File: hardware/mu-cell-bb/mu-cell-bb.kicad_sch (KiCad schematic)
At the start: 73 parts, among them IC1 SX1255, J1 TX, J2 RX, J3 EXT_CLK, J4 RPi GPIO, J5 IO, Q1 BC817-40W, Q2 BC817-40W, U1 24LC256, U2 LDK130M33R, Y1 32MHz

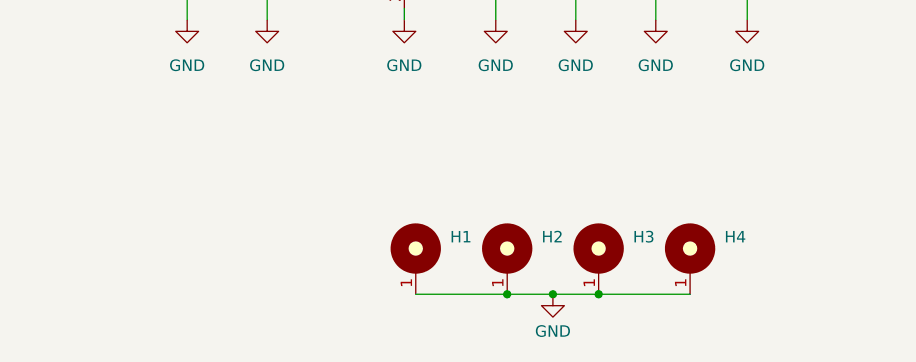
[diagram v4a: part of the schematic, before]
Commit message: added PCB changes and parts
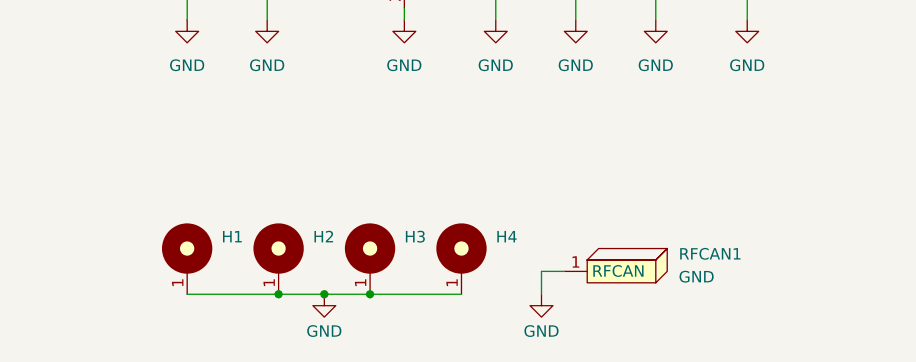
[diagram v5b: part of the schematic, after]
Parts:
- added RFCAN1: GND, parts:2118707-4 CAN, symbol parts:RFCAN
- J5: footprint Connector_IDC:IDC-Header_2x06_P2.54mm_Vertical -> Connector_IDC:IDC-Header_2x06_P2.54mm_Horizontal
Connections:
- net GND: now also RFCAN1.1 (RFCAN)
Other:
- moved on the sheet: H1, H2, H3, H4
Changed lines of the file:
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@@
 	)
 	(junction
-		(at 148.59 186.69)
+		(at 123.19 186.69)
 		(diameter 0)
 		(color 0 0 0 0)
 	)
 	(junction
-		(at 138.43 186.69)
+		(at 113.03 186.69)
 		(diameter 0)
 		(color 0 0 0 0)
@@
 	)
 	(junction
-		(at 143.51 186.69)
+		(at 118.11 186.69)
 		(diameter 0)
 		(color 0 0 0 0)
@@
 	(wire
 		(pts
+			(xy 142.24 184.15) (xy 144.78 184.15)
+		)
+		(stroke
+			(width 0)
+			(type default)
+		)
+	)
+	(wire
+		(pts
 			(xy 40.64 60.96) (xy 40.64 64.77)
 		)
@@
 	(wire
 		(pts
-			(xy 148.59 186.69) (xy 158.75 186.69)
+			(xy 123.19 186.69) (xy 133.35 186.69)
 		)
 		(stroke
@@
 	(wire
 		(pts
+			(xy 142.24 186.69) (xy 142.24 184.15)
+		)
+		(stroke
+			(width 0)
+			(type default)
+		)
+	)
+	(wire
+		(pts
 			(xy 163.83 76.2) (xy 179.07 76.2)
 		)
@@
 	(wire
 		(pts
-			(xy 138.43 186.69) (xy 143.51 186.69)
+			(xy 113.03 186.69) (xy 118.11 186.69)
 		)
 		(stroke
@@
 	(wire
 		(pts
-			(xy 128.27 186.69) (xy 138.43 186.69)
+			(xy 102.87 186.69) (xy 113.03 186.69)
 		)
 		(stroke
@@
 	(wire
 		(pts
-			(xy 143.51 186.69) (xy 148.59 186.69)
+			(xy 118.11 186.69) (xy 123.19 186.69)
 		)
 		(stroke
@@
 	(symbol
 		(lib_id "PCM_SL_Mechanical:MountingHole_M3_3.2mm_Pad")
-		(at 148.59 181.61 0)
+		(at 123.19 181.61 0)
 		(unit 1)
 		(exclude_from_sim no)
@@
 		(fields_autoplaced yes)
 		(property "Reference" "H3"
-			(at 152.4 180.3399 0)
+			(at 127 180.3399 0)
 			(effects
 				(font
@@
 		)
 		(property "Value" "MountingHole_M3_3.2mm_Pad"
-			(at 152.4 182.8799 0)
+			(at 127 182.8799 0)
 			(effects
 				(font
@@
 		)
 		(property "Footprint" "MountingHole:MountingHole_3.2mm_M3_DIN965_Pad"
-			(at 148.59 185.42 0)
+			(at 123.19 185.42 0)
 			(effects
 				(font
@@
 		)
 		(property "Datasheet" ""
-			(at 148.59 181.61 0)
+			(at 123.19 181.61 0)
 			(effects
 				(font
@@
 		)
 		(property "Description" "3.2mm Diameter Mounting Hole Pad (M3)"
-			(at 148.59 181.61 0)
+			(at 123.19 181.61 0)
 			(effects
 				(font
@@
 	(symbol
 		(lib_id "PCM_SL_Mechanical:MountingHole_M3_3.2mm_Pad")
-		(at 128.27 181.61 0)
+		(at 102.87 181.61 0)
 		(unit 1)
 		(exclude_from_sim no)
@@
 		(fields_autoplaced yes)
 		(property "Reference" "H1"
-			(at 132.08 180.3399 0)
+			(at 106.68 180.3399 0)
 			(effects
 				(font
@@
 		)
 		(property "Value" "MountingHole_M3_3.2mm_Pad"
-			(at 132.08 182.8799 0)
+			(at 106.68 182.8799 0)
 			(effects
 				(font
@@
 		)
 		(property "Footprint" "MountingHole:MountingHole_3.2mm_M3_DIN965_Pad"
-			(at 128.27 185.42 0)
+			(at 102.87 185.42 0)
 			(effects
 				(font
@@
 		)
 		(property "Datasheet" ""
-			(at 128.27 181.61 0)
+			(at 102.87 181.61 0)
 			(effects
 				(font
@@
 		)
 		(property "Description" "3.2mm Diameter Mounting Hole Pad (M3)"
-			(at 128.27 181.61 0)
+			(at 102.87 181.61 0)
 			(effects
 				(font
@@
 	(symbol
 		(lib_id "power:GND")
-		(at 143.51 186.69 0)
+		(at 118.11 186.69 0)
 		(unit 1)
 		(exclude_from_sim no)
@@
 		(fields_autoplaced yes)
 		(property "Reference" "#PWR044"
-			(at 143.51 193.04 0)
+			(at 118.11 193.04 0)
 			(effects
 				(font
@@
 		)
 		(property "Value" "GND"
-			(at 143.51 190.8231 0)
+			(at 118.11 190.8231 0)
 			(effects
 				(font
@@
 		)
 		(property "Footprint" ""
-			(at 143.51 186.69 0)
+			(at 118.11 186.69 0)
 			(effects
 				(font
@@
 		)
 		(property "Datasheet" ""
-			(at 143.51 186.69 0)
+			(at 118.11 186.69 0)
 			(effects
 				(font
@@
 		)
 		(property "Description" "Power symbol creates a global label with name \"GND\" , ground"
-			(at 143.51 186.69 0)
+			(at 118.11 186.69 0)
 			(effects
 				(font
@@
 	)
 	(symbol
+		(lib_id "power:GND")
+		(at 142.24 186.69 0)
+		(unit 1)
+		(exclude_from_sim no)
+		(in_bom yes)
+		(on_board yes)
+		(dnp no)
+		(fields_autoplaced yes)
+		(property "Reference" "#PWR061"
+			(at 142.24 193.04 0)
+			(effects
+				(font
+					(size 1.27 1.27)
+				)
+				(hide yes)
+			)
+		)
+		(property "Value" "GND"
+			(at 142.24 190.8231 0)
+			(effects
+				(font
+					(size 1.27 1.27)
+				)
+			)
+		)
+		(property "Footprint" ""
+			(at 142.24 186.69 0)
+			(effects
+				(font
+					(size 1.27 1.27)
+				)
+				(hide yes)
+			)
+		)
+		(property "Datasheet" ""
+			(at 142.24 186.69 0)
+			(effects
+				(font
+					(size 1.27 1.27)
+				)
+				(hide yes)
+			)
+		)
+		(property "Description" "Power symbol creates a global label with name \"GND\" , ground"
+			(at 142.24 186.69 0)
+			(effects
+				(font
+					(size 1.27 1.27)
+				)
+				(hide yes)
+			)
+		)
+		(pin "1"
+		)
+		(instances
+			(project "mu-cell-bb"
+				(path "/564c8f3e-4a0a-4bb3-921f-1318a09780f9"
+					(reference "#PWR061")
+					(unit 1)
+				)
+			)
+		)
+	)
+	(symbol
 		(lib_id "Device:C_Small")
 		(at 102.87 36.83 0)
@@
 	(symbol
 		(lib_id "PCM_SL_Mechanical:MountingHole_M3_3.2mm_Pad")
-		(at 138.43 181.61 0)
+		(at 113.03 181.61 0)
 		(unit 1)
 		(exclude_from_sim no)
@@
 		(fields_autoplaced yes)
 		(property "Reference" "H2"
-			(at 142.24 180.3399 0)
+			(at 116.84 180.3399 0)
 			(effects
 				(font
@@
 		)
 		(property "Value" "MountingHole_M3_3.2mm_Pad"
-			(at 142.24 182.8799 0)
+			(at 116.84 182.8799 0)
 			(effects
 				(font
@@
 		)
 		(property "Footprint" "MountingHole:MountingHole_3.2mm_M3_DIN965_Pad"
-			(at 138.43 185.42 0)
+			(at 113.03 185.42 0)
 			(effects
 				(font
@@
 		)
 		(property "Datasheet" ""
-			(at 138.43 181.61 0)
+			(at 113.03 181.61 0)
 			(effects
 				(font
@@
 		)
 		(property "Description" "3.2mm Diameter Mounting Hole Pad (M3)"
-			(at 138.43 181.61 0)
+			(at 113.03 181.61 0)
 			(effects
 				(font
@@
 	)
 	(symbol
+		(lib_id "parts:RFCAN")
+		(at 151.13 184.15 0)
+		(unit 1)
+		(exclude_from_sim no)
+		(in_bom yes)
+		(on_board yes)
+		(dnp no)
+		(fields_autoplaced yes)
+		(property "Reference" "RFCAN1"
+			(at 157.48 182.2449 0)
+			(effects
+				(font
+					(size 1.27 1.27)
+				)
+				(justify left)
+			)
+		)
+		(property "Value" "GND"
+			(at 157.48 184.7849 0)
+			(effects
+				(font
+					(size 1.27 1.27)
+				)
+				(justify left)
+			)
+		)
+		(property "Footprint" "parts:2118707-4 CAN"
+			(at 151.13 184.15 0)
+			(effects
+				(font
+					(size 1.27 1.27)
+				)
+				(hide yes)
+			)
+		)
+		(property "Datasheet" ""
+			(at 151.13 184.15 0)
+			(effects
+				(font
+					(size 1.27 1.27)
+				)
+				(hide yes)
+			)
+		)
+		(property "Description" ""
+			(at 151.13 184.15 0)
+			(effects
+				(font
+					(size 1.27 1.27)
+				)
+				(hide yes)
+			)
+		)
+		(pin "1"
+		)
+		(instances
+			(project ""
+				(path "/564c8f3e-4a0a-4bb3-921f-1318a09780f9"
+					(reference "RFCAN1")
+					(unit 1)
+				)
+			)
+		)
+	)
+	(symbol
 		(lib_id "power:GND")
 		(at 30.48 40.64 0)
@@
 	(symbol
 		(lib_id "PCM_SL_Mechanical:MountingHole_M3_3.2mm_Pad")
-		(at 158.75 181.61 0)
+		(at 133.35 181.61 0)
 		(unit 1)
 		(exclude_from_sim no)
@@
 		(fields_autoplaced yes)
 		(property "Reference" "H4"
-			(at 162.56 180.3399 0)
+			(at 137.16 180.3399 0)
 			(effects
 				(font
@@
 		)
 		(property "Value" "MountingHole_M3_3.2mm_Pad"
-			(at 162.56 182.8799 0)
+			(at 137.16 182.8799 0)
 			(effects
 				(font
@@
 		)
 		(property "Footprint" "MountingHole:MountingHole_3.2mm_M3_DIN965_Pad"
-			(at 158.75 185.42 0)
+			(at 133.35 185.42 0)
 			(effects
 				(font
@@
 		)
 		(property "Datasheet" ""
-			(at 158.75 181.61 0)
+			(at 133.35 181.61 0)
 			(effects
 				(font
@@
 		)
 		(property "Description" "3.2mm Diameter Mounting Hole Pad (M3)"
-			(at 158.75 181.61 0)
+			(at 133.35 181.61 0)
 			(effects
 				(font
@@
 			)
 		)
-		(property "Footprint" "Connector_IDC:IDC-Header_2x06_P2.54mm_Vertical"
+		(property "Footprint" "Connector_IDC:IDC-Header_2x06_P2.54mm_Horizontal"
 			(at 247.65 69.85 0)
 			(effects

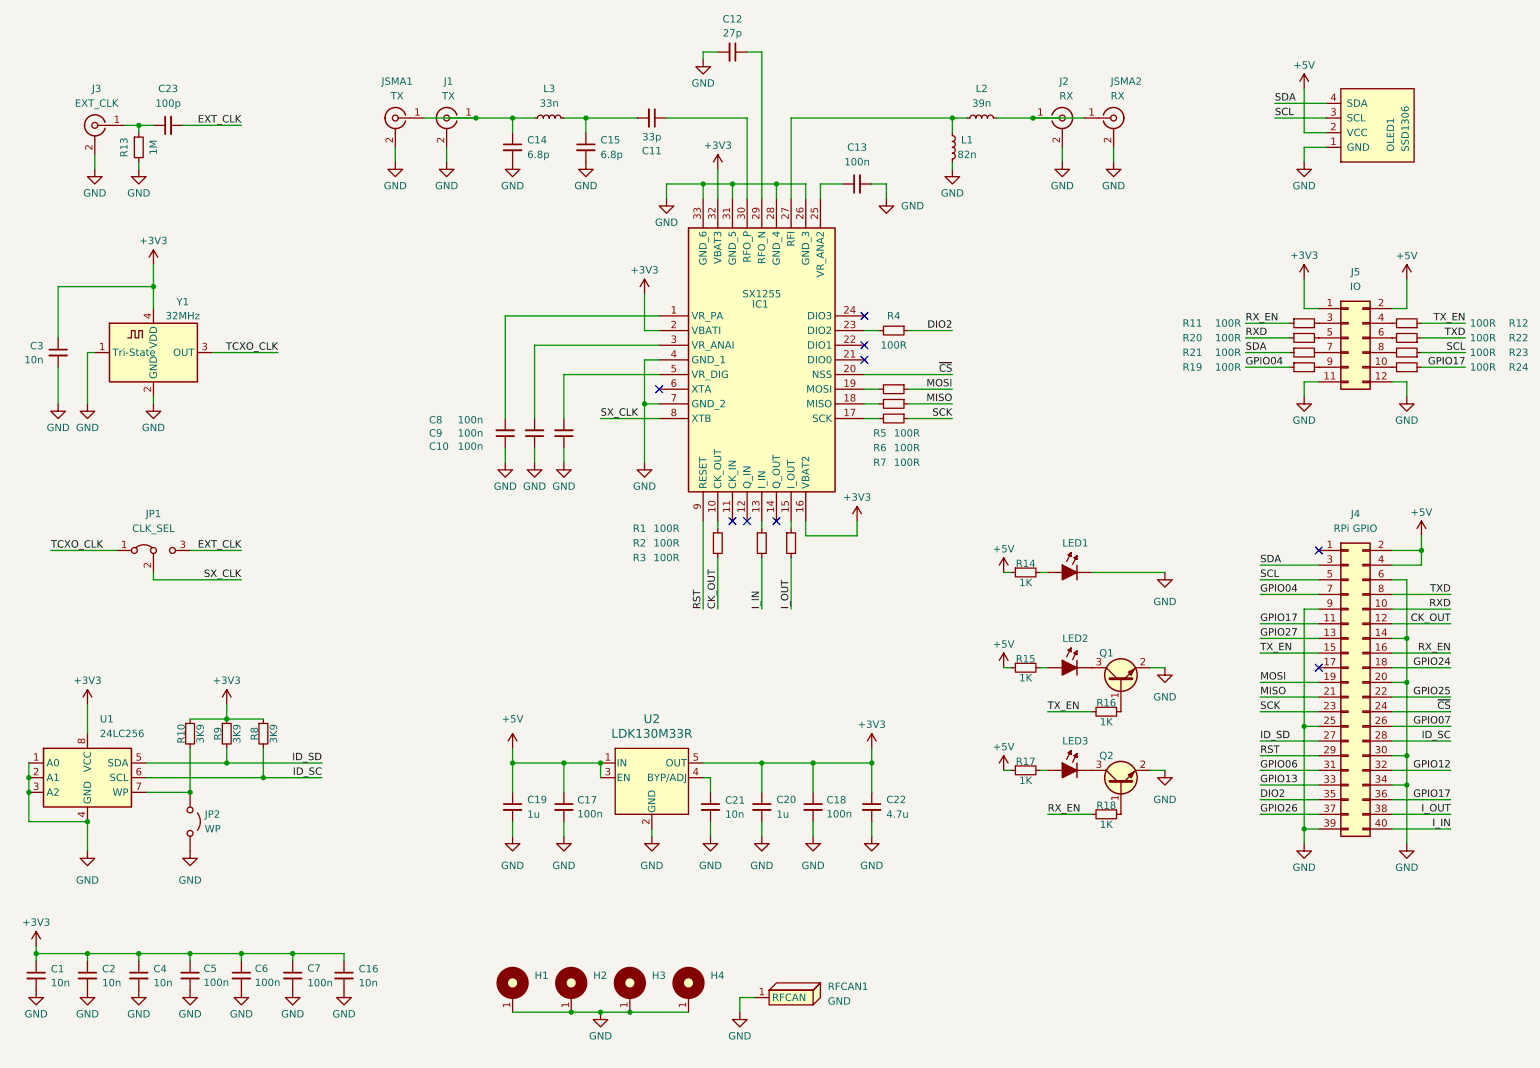
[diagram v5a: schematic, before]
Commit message: updated footprints
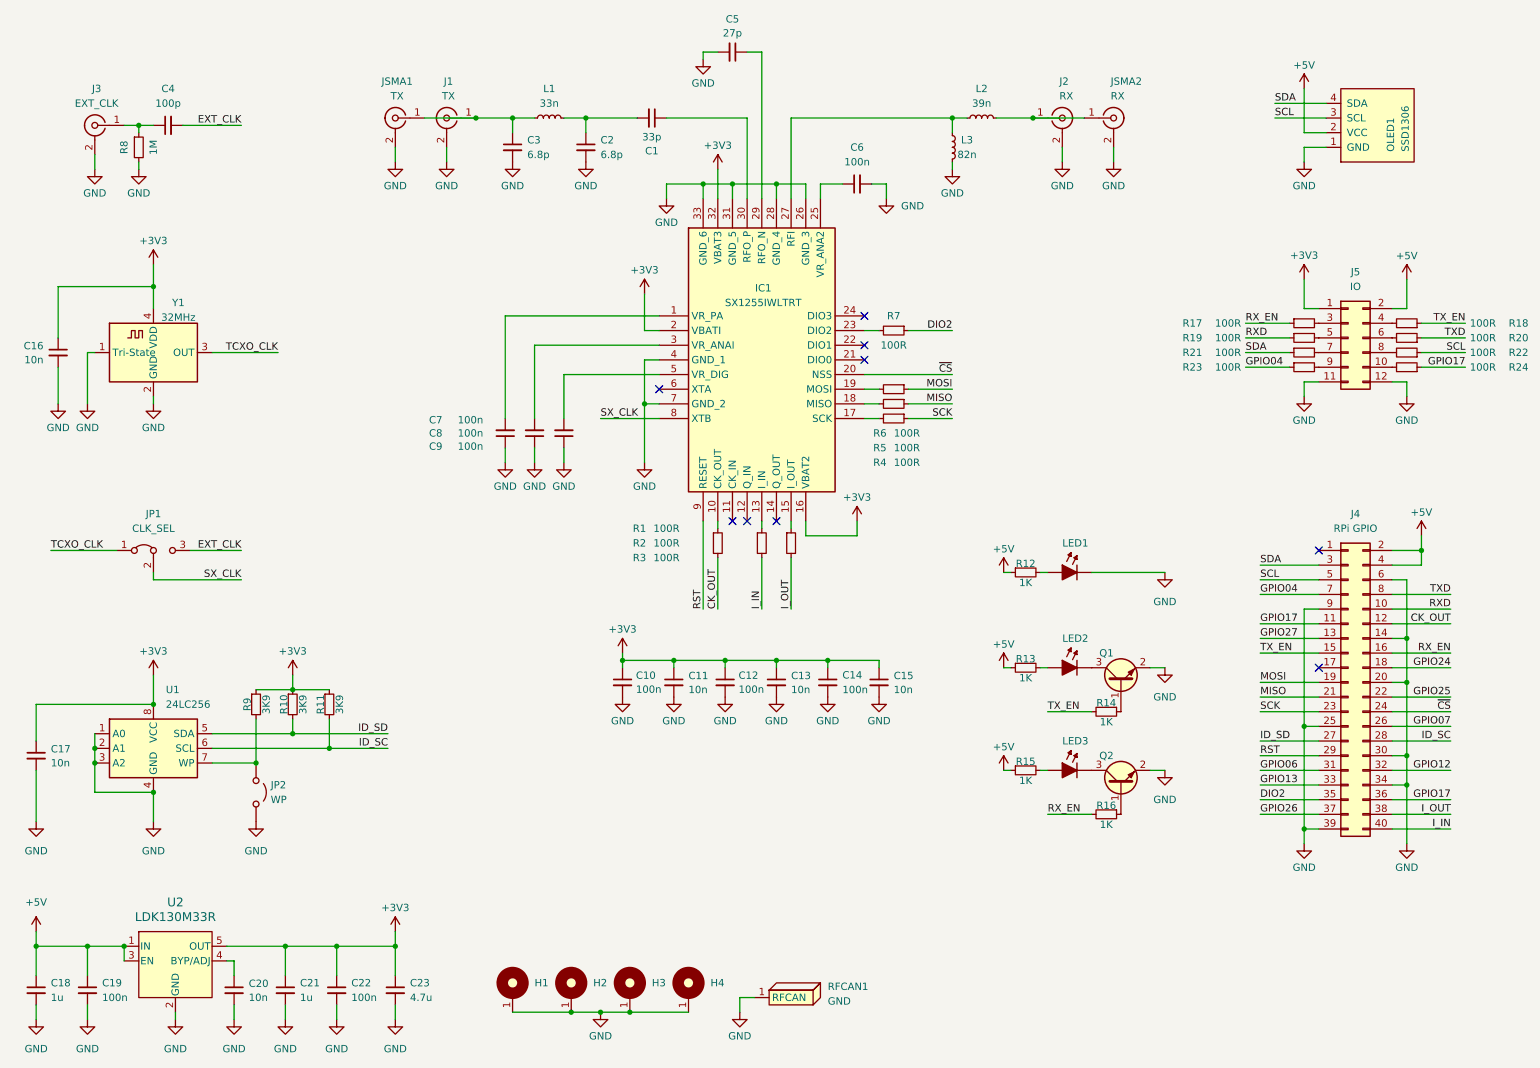
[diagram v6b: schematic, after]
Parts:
- removed C16, C2, C4: 10n, Capacitor_SMD:C_0603_1608Metric, symbol Device:C_Small
- removed C5, C6, C7: 100n, Capacitor_SMD:C_0603_1608Metric, symbol Device:C_Small
- removed IC1: SX1255, parts:QFN50P500X500X80-33N-D, symbol SX1255:SX1255IWLTRT
- removed Y1: 32MHz, Oscillator:Oscillator_SMD_ECS_2520MV-xxx-xx-4Pin_2.5x2.0mm, symbol Oscillator:ECS-2520MV-xxx-xx
- added C10, C12, C14: 100n, Capacitor_SMD:C_0402_1005Metric_Pad0.74x0.62mm_HandSolder, symbol Device:C_Small
- added C13, C15, C17: 10n, Capacitor_SMD:C_0402_1005Metric_Pad0.74x0.62mm_HandSolder, symbol Device:C_Small
- added IC1: SX1255IWLTRT, parts:QFN50P500X500X80-33N-D, symbol parts:SX1255IWLTRT
- added Y1: 32MHz, parts:Oscillator_SMD_ECS_2520MV-xxx-xx-4Pin_2.5x2.0mm, symbol parts:ECS-2520MV-xxx-xx
- C1: renamed from C11; footprint Capacitor_SMD:C_0603_1608Metric -> Capacitor_SMD:C_0402_1005Metric_Pad0.74x0.62mm_HandSolder
- C11: renamed from C1; footprint Capacitor_SMD:C_0603_1608Metric -> Capacitor_SMD:C_0402_1005Metric_Pad0.74x0.62mm_HandSolder
- C16: renamed from C3; footprint Capacitor_SMD:C_0603_1608Metric -> Capacitor_SMD:C_0402_1005Metric_Pad0.74x0.62mm_HandSolder
- C18: renamed from C19; footprint Capacitor_SMD:C_0603_1608Metric -> Capacitor_SMD:C_0402_1005Metric_Pad0.74x0.62mm_HandSolder
- C19: renamed from C17; footprint Capacitor_SMD:C_0603_1608Metric -> Capacitor_SMD:C_0402_1005Metric_Pad0.74x0.62mm_HandSolder
- C2: renamed from C15; footprint Capacitor_SMD:C_0603_1608Metric -> Capacitor_SMD:C_0402_1005Metric_Pad0.74x0.62mm_HandSolder
- C20: renamed from C21; footprint Capacitor_SMD:C_0603_1608Metric -> Capacitor_SMD:C_0402_1005Metric_Pad0.74x0.62mm_HandSolder
- C21: renamed from C20; footprint Capacitor_SMD:C_0603_1608Metric -> Capacitor_SMD:C_0402_1005Metric_Pad0.74x0.62mm_HandSolder
- C22: renamed from C18; footprint Capacitor_SMD:C_0603_1608Metric -> Capacitor_SMD:C_0402_1005Metric_Pad0.74x0.62mm_HandSolder
- C23: renamed from C22; footprint Capacitor_SMD:C_0603_1608Metric -> Capacitor_SMD:C_0402_1005Metric_Pad0.74x0.62mm_HandSolder
- C3: renamed from C14; footprint Capacitor_SMD:C_0603_1608Metric -> Capacitor_SMD:C_0402_1005Metric_Pad0.74x0.62mm_HandSolder
- C4: renamed from C23; footprint Capacitor_SMD:C_0603_1608Metric -> Capacitor_SMD:C_0402_1005Metric_Pad0.74x0.62mm_HandSolder
- C5: renamed from C12; footprint Capacitor_SMD:C_0603_1608Metric -> Capacitor_SMD:C_0402_1005Metric_Pad0.74x0.62mm_HandSolder
- C6: renamed from C13; footprint Capacitor_SMD:C_0603_1608Metric -> Capacitor_SMD:C_0402_1005Metric_Pad0.74x0.62mm_HandSolder
- C7: renamed from C8; footprint Capacitor_SMD:C_0603_1608Metric -> Capacitor_SMD:C_0402_1005Metric_Pad0.74x0.62mm_HandSolder
- C8: renamed from C9; footprint Capacitor_SMD:C_0603_1608Metric -> Capacitor_SMD:C_0402_1005Metric_Pad0.74x0.62mm_HandSolder
- C9: renamed from C10; footprint Capacitor_SMD:C_0603_1608Metric -> Capacitor_SMD:C_0402_1005Metric_Pad0.74x0.62mm_HandSolder
- H1, H2, H3, H4: footprint MountingHole:MountingHole_3.2mm_M3_DIN965_Pad -> PCM_SL_Mechanical:MountingHole_3.2mm_Pad
- J3: footprint (none) -> parts:U.FL_Vertical_GND
- L1: renamed from L3; footprint Inductor_SMD:L_0603_1608Metric -> Inductor_SMD:L_0402_1005Metric_Pad0.77x0.64mm_HandSolder
- L2: footprint Inductor_SMD:L_0603_1608Metric -> Inductor_SMD:L_0402_1005Metric_Pad0.77x0.64mm_HandSolder
- L3: renamed from L1; footprint Inductor_SMD:L_0603_1608Metric -> Inductor_SMD:L_0402_1005Metric_Pad0.77x0.64mm_HandSolder
- LED1, LED2, LED3: footprint LED_SMD:LED_0603_1608Metric -> PCM_LED_SMD_AKL:LED_0402_1005Metric_Pad0.77x0.64mm
- Q1, Q2: footprint Package_TO_SOT_SMD:SOT-323_SC-70_Handsoldering -> Package_TO_SOT_SMD:SOT-323_SC-70
- R1, R2, R21, R24, R3: footprint Resistor_SMD:R_0603_1608Metric -> Resistor_SMD:R_0402_1005Metric_Pad0.72x0.64mm_HandSolder
- R10: renamed from R9; footprint Resistor_SMD:R_0603_1608Metric -> Resistor_SMD:R_0402_1005Metric_Pad0.72x0.64mm_HandSolder
- R11: renamed from R8; footprint Resistor_SMD:R_0603_1608Metric -> Resistor_SMD:R_0402_1005Metric_Pad0.72x0.64mm_HandSolder
- R12: renamed from R14; footprint Resistor_SMD:R_0603_1608Metric -> Resistor_SMD:R_0402_1005Metric_Pad0.72x0.64mm_HandSolder
- R13: renamed from R15; footprint Resistor_SMD:R_0603_1608Metric -> Resistor_SMD:R_0402_1005Metric_Pad0.72x0.64mm_HandSolder
- R14: renamed from R16; footprint Resistor_SMD:R_0603_1608Metric -> Resistor_SMD:R_0402_1005Metric_Pad0.72x0.64mm_HandSolder
- R15: renamed from R17; footprint Resistor_SMD:R_0603_1608Metric -> Resistor_SMD:R_0402_1005Metric_Pad0.72x0.64mm_HandSolder
- R16: renamed from R18; footprint Resistor_SMD:R_0603_1608Metric -> Resistor_SMD:R_0402_1005Metric_Pad0.72x0.64mm_HandSolder
- R17: renamed from R11; footprint Resistor_SMD:R_0603_1608Metric -> Resistor_SMD:R_0402_1005Metric_Pad0.72x0.64mm_HandSolder
- R18: renamed from R12; footprint Resistor_SMD:R_0603_1608Metric -> Resistor_SMD:R_0402_1005Metric_Pad0.72x0.64mm_HandSolder
- R19: renamed from R20; footprint Resistor_SMD:R_0603_1608Metric -> Resistor_SMD:R_0402_1005Metric_Pad0.72x0.64mm_HandSolder
- R20: renamed from R22; footprint Resistor_SMD:R_0603_1608Metric -> Resistor_SMD:R_0402_1005Metric_Pad0.72x0.64mm_HandSolder
- R22: renamed from R23; footprint Resistor_SMD:R_0603_1608Metric -> Resistor_SMD:R_0402_1005Metric_Pad0.72x0.64mm_HandSolder
- R23: renamed from R19; footprint Resistor_SMD:R_0603_1608Metric -> Resistor_SMD:R_0402_1005Metric_Pad0.72x0.64mm_HandSolder
- R4: renamed from R7; footprint Resistor_SMD:R_0603_1608Metric -> Resistor_SMD:R_0402_1005Metric_Pad0.72x0.64mm_HandSolder
- R5: renamed from R6; footprint Resistor_SMD:R_0603_1608Metric -> Resistor_SMD:R_0402_1005Metric_Pad0.72x0.64mm_HandSolder
- R6: renamed from R5; footprint Resistor_SMD:R_0603_1608Metric -> Resistor_SMD:R_0402_1005Metric_Pad0.72x0.64mm_HandSolder
- R7: renamed from R4; footprint Resistor_SMD:R_0603_1608Metric -> Resistor_SMD:R_0402_1005Metric_Pad0.72x0.64mm_HandSolder
- R8: renamed from R13; footprint Resistor_SMD:R_0603_1608Metric -> Resistor_SMD:R_0402_1005Metric_Pad0.72x0.64mm_HandSolder
- R9: renamed from R10; footprint Resistor_SMD:R_0603_1608Metric -> Resistor_SMD:R_0402_1005Metric_Pad0.72x0.64mm_HandSolder
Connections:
- net +3V3: now also C10.1, C12.1, C13.1, C14.1, C15.1, C17.1, IC1.16 (VBAT2), IC1.2 (VBATI), IC1.32 (VBAT3), Y1.4 (VDD)
- net GND: now also C10.2, C12.2, C13.2, C14.2, C15.2, C17.2, IC1.26 (GND_3), IC1.28 (GND_4), IC1.31 (GND_5), IC1.33 (GND_6), IC1.4 (GND_1), IC1.7 (GND_2), Y1.1 (Tri-State), Y1.2 (GND)
- net RST: now also IC1.9 (RESET)
- net SX_CLK: now also IC1.8 (XTB)
- net TCXO_CLK: now also Y1.3 (OUT)
- net ~{CS}: now also IC1.20 (NSS)
- net at C7.2: now also IC1.1 (VR_PA)
- net at L2.2, L3.2: now also IC1.27 (RFI)
- net at C8.2: now also IC1.3 (VR_ANAI)
- net at C6.1: now also IC1.25 (VR_ANA2)
- net at R7.2: now also IC1.23 (DIO2)
- net at C5.1: now also IC1.29 (RFO_N)
- net at C1.1: now also IC1.30 (RFO_P)
- net at R4.2: now also IC1.17 (SCK)
- net at R3.1: now also IC1.15 (I_OUT)
- net at R6.2: now also IC1.19 (MOSI)
- net at C9.2: now also IC1.5 (VR_DIG)
- net at R1.1: now also IC1.10 (CK_OUT)
- net at R2.1: now also IC1.13 (I_IN)
- net at R5.2: now also IC1.18 (MISO)
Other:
- moved on the sheet: C11, C18, C19, C20, C21, C22, C23, JP2, R10, R11, R9, U1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
